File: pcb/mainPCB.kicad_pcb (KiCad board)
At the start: 4 copper layers, 160 x 73.2 mm, 167 parts, among them IC1 FXL6408UMX, IC2 ATA6561-GAQW-N, IC3 ICL3221EIVZ, J1 PTSM-Header-Horizontal-6, J10 Conn_01x08_Female, J11 Conn_01x08_Female, J12 Conn_02x02_Odd_Even, J13 SM04B-SRSS-TB(LF)(SN), J14 USB_B_Micro, J15 RJ45_Amphenol_RJMG1BD3B8K1ANR, J16 DB9_Male_MountingHoles, J17 SM04B-SRSS-TB(LF)(SN), J18 PTSM-Header-Horizontal-2, J3 PTSM-Header-Horizontal-7, J4 CCA-Header-Horizontal-4, J5 PTSM-Header-Horizontal-5, J7 Conn_01x04_Male, J8 Conn_01x04_Male, J9 Conn_01x08_Female, K1 CP1SA-12V-Z, K2 CP1SA-12V-Z, Q1 BC817-40,215, Q2 BC817-40,215, SW1 SW_Push, U1 ESP32-WROOM-32, U10 NUD3124LT1G, U11 LAN8720A, U12 LSM9DS1, U2 AZ1117-3.3, U3 VNH7070AS, U4 ADS1115IDGS, U5 VNH7070AS, U6 PCA9306DCTR, U7 TPD3E001DRLR, U8 CP2102N-A01-GQFN24, U9 VNH7070AS

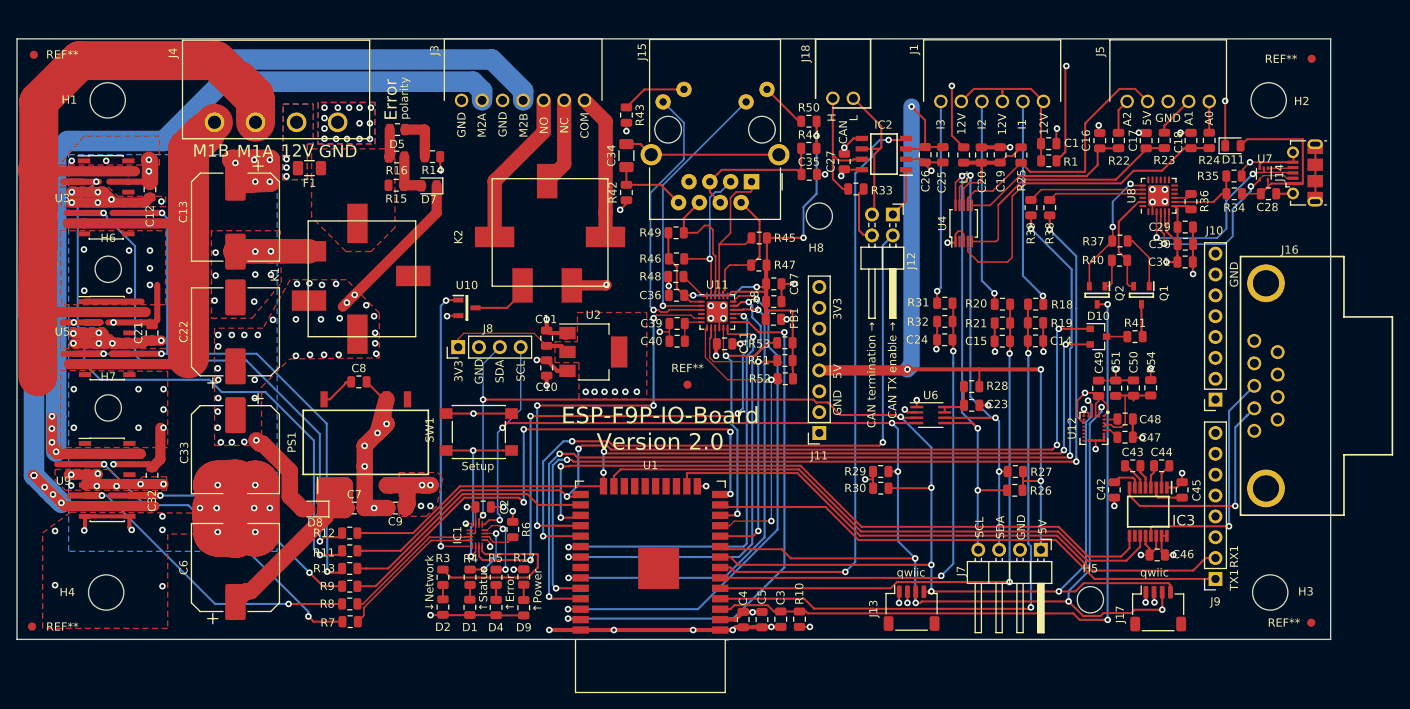
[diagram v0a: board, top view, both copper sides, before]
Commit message: Moved mounting hole. fixes #1
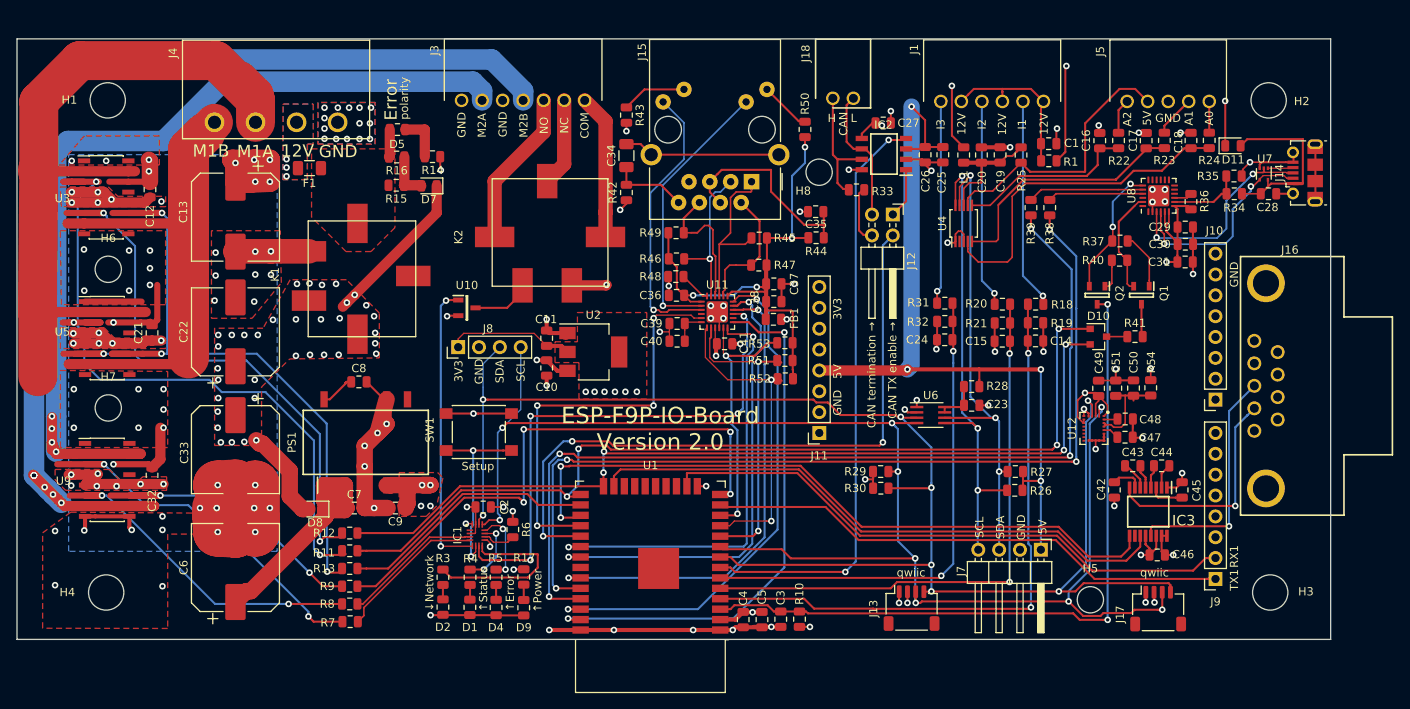
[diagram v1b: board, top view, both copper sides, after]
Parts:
- removed ?: , 
- removed REF** (x5): Fiducial_1mm_Dia_2mm_Outer, Fiducial:Fiducial_1mm_Dia_2mm_Outer
- moved R44 10.9 mm to (114.8, 61.7), turned to 180 degrees
- moved C27 6.66 mm to (123.0, 47.7), turned to 180 degrees
- moved H8 5.35 mm to (115.2, 53.7)
- moved C35 4.61 mm to (114.7, 58.5), turned to 0 degrees
- moved R50 1.10 mm to (113.4, 48.5), turned to 270 degrees
- moved R33 0.12 mm to (119.7, 55.8)
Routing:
- net Net-(C35-Pad2): track 18.3 -> 25.1 mm
- net /LAN8720/+3V3LAN: track 73.6 -> 70.8 mm
- net Net-(IC2-Pad6): track 18.2 -> 17.0 mm
- net Net-(IC2-Pad7): track 16.1 -> 15.1 mm
- net /CAN_RXD: track 73.1 -> 72.5 mm
- net GND: track 280.2 -> 280.4 mm, vias 116 -> 117

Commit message: Minor cleanups
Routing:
- net GND: track 280.4 -> 288.7 mm, vias 117 -> 115
- net +3V3: track 82.3 -> 85.2 mm
- net /CAN_RXD: track 72.5 -> 74.7 mm
- net Net-(IC2-Pad6): track 17.0 -> 18.0 mm, vias 0 -> 1

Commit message: Minor cleanups
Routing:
- net GND: track 288.7 -> 298.2 mm, vias 115 -> 112
- net Net-(C28-Pad1): track 24.5 -> 23.9 mm
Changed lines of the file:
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@@
     (thickness 1.6)
     (drawings 57)
-    (tracks 1815)
+    (tracks 1810)
     (zones 0)
     (modules 161)
@@
   (segment (start 128.0795 52.7685) (end 128.8415 53.5305) (width 0.25) (layer F.Cu) (net 1))
   (segment (start 128.0795 52.5145) (end 130.2385 52.5145) (width 0.25) (layer F.Cu) (net 1))
-  (via (at 159.1945 48.895) (size 0.8) (drill 0.4) (layers F.Cu B.Cu) (net 1))
-  (via (at 154.1145 48.895) (size 0.8) (drill 0.4) (layers F.Cu B.Cu) (net 1))
-  (segment (start 155.1305 48.925) (end 154.1445 48.925) (width 0.25) (layer F.Cu) (net 1))
-  (segment (start 154.1445 48.925) (end 154.1145 48.895) (width 0.25) (layer F.Cu) (net 1))
-  (via (at 149.225 48.006) (size 0.8) (drill 0.4) (layers F.Cu B.Cu) (net 1))
   (via (at 138.43 50.673) (size 0.8) (drill 0.4) (layers F.Cu B.Cu) (net 1))
   (segment (start 134.9375 50.673) (end 138.43 50.673) (width 0.5) (layer F.Cu) (net 1))
@@
   (segment (start 175.62068 50.4198) (end 175.62068 56.8198) (width 0.25) (layer F.Cu) (net 1))
   (segment (start 172.95422 51.29212) (end 172.95422 52.49212) (width 0.25) (layer F.Cu) (net 1))
-  (segment (start 172.02922 52.49212) (end 172.95422 52.49212) (width 0.25) (layer F.Cu) (net 1))
-  (segment (start 168.83672 53.21912) (end 168.83672 52.74412) (width 0.25) (layer F.Cu) (net 1))
-  (segment (start 168.83672 52.74412) (end 169.08872 52.49212) (width 0.25) (layer F.Cu) (net 1))
   (segment (start 170.70372 56.80412) (end 170.70372 56.84012) (width 0.25) (layer F.Cu) (net 1))
   (segment (start 172.91422 56.33212) (end 172.95422 56.29212) (width 0.25) (layer F.Cu) (net 1))
@@
   (segment (start 166.76672 53.37312) (end 167.64772 52.49212) (width 0.2) (layer F.Cu) (net 1))
   (segment (start 166.76672 54.17312) (end 166.76672 53.37312) (width 0.2) (layer F.Cu) (net 1))
-  (segment (start 169.08872 52.49212) (end 169.27322 52.49212) (width 0.25) (layer F.Cu) (net 1))
-  (segment (start 169.27322 52.49212) (end 171.96572 52.49212) (width 0.25) (layer F.Cu) (net 1))
-  (segment (start 167.64772 52.49212) (end 169.27322 52.49212) (width 0.2) (layer F.Cu) (net 1))
-  (via (at 167.64772 52.49212) (size 0.8) (drill 0.4) (layers F.Cu B.Cu) (net 1))
   (via (at 160.7185 66.1035) (size 0.8) (drill 0.4) (layers F.Cu B.Cu) (net 1))
   (segment (start 160.7035 60.3885) (end 160.7035 66.0885) (width 0.25) (layer F.Cu) (net 1))
@@
   (segment (start 149.322 48.895) (end 149.352 48.925) (width 0.25) (layer F.Cu) (net 1))
   (segment (start 149.225 48.798) (end 149.352 48.925) (width 0.25) (layer F.Cu) (net 1))
-  (segment (start 149.225 48.006) (end 149.225 48.798) (width 0.25) (layer F.Cu) (net 1))
   (segment (start 160.4495 48.895) (end 160.4645 48.91) (width 0.25) (layer F.Cu) (net 1))
-  (segment (start 159.1945 48.895) (end 160.4495 48.895) (width 0.25) (layer F.Cu) (net 1))
   (segment (start 129.54 75.176509) (end 129.451436 75.265073) (width 0.25) (layer F.Cu) (net 1))
   (segment (start 129.54 71.882) (end 129.54 75.176509) (width 0.25) (layer F.Cu) (net 1))
@@
   (segment (start 122.633 50.144799) (end 123.90676 48.871039) (width 0.25) (layer F.Cu) (net 1))
   (segment (start 122.633 52.1335) (end 122.633 50.144799) (width 0.25) (layer F.Cu) (net 1))
+  (segment (start 149.908237 49.481237) (end 149.352 48.925) (width 0.25) (layer F.Cu) (net 1))
+  (segment (start 150.27704 49.85004) (end 149.908237 49.481237) (width 0.25) (layer F.Cu) (net 1))
+  (segment (start 160.4645 48.91) (end 159.52446 49.85004) (width 0.25) (layer F.Cu) (net 1))
+  (segment (start 159.52446 49.85004) (end 155.00096 49.85004) (width 0.25) (layer F.Cu) (net 1))
+  (segment (start 155.00096 49.85004) (end 153.95448 49.85004) (width 0.25) (layer F.Cu) (net 1))
+  (segment (start 155.0035 49.8475) (end 155.0035 48.925) (width 0.25) (layer F.Cu) (net 1))
+  (segment (start 153.95448 49.85004) (end 150.27704 49.85004) (width 0.25) (layer F.Cu) (net 1))
+  (via (at 153.95448 49.85004) (size 0.8) (drill 0.4) (layers F.Cu B.Cu) (net 1))
+  (segment (start 168.83672 53.21912) (end 168.83672 52.49212) (width 0.2) (layer F.Cu) (net 1))
+  (segment (start 172.89072 52.49212) (end 168.83672 52.49212) (width 0.25) (layer F.Cu) (net 1))
+  (segment (start 168.83672 52.49212) (end 167.64772 52.49212) (width 0.25) (layer F.Cu) (net 1))
   (via (at 50.292 54.2036) (size 0.8) (drill 0.4) (layers F.Cu B.Cu) (net 2))
   (via (at 50.292 53.1368) (size 0.8) (drill 0.4) (layers F.Cu B.Cu) (net 2))
@@
   (segment (start 167.760769 55.436976) (end 167.760769 56.002661) (width 0.25) (layer B.Cu) (net 97))
   (segment (start 167.760769 56.002661) (end 165.5445 58.21893) (width 0.25) (layer B.Cu) (net 97))
-  (segment (start 169.33672 53.59412) (end 169.33672 53.21912) (width 0.15) (layer F.Cu) (net 98))
-  (segment (start 169.461721 53.719121) (end 169.33672 53.59412) (width 0.15) (layer F.Cu) (net 98))
-  (segment (start 171.992721 53.719121) (end 169.461721 53.719121) (width 0.15) (layer F.Cu) (net 98))
-  (segment (start 172.95422 53.79212) (end 172.12922 53.79212) (width 0.15) (layer F.Cu) (net 98))
-  (segment (start 172.12922 53.79212) (end 172.056221 53.719121) (width 0.15) (layer F.Cu) (net 98))
   (via (at 168.00322 53.91912) (size 0.8) (drill 0.4) (layers F.Cu B.Cu) (net 98))
-  (segment (start 168.178219 53.744121) (end 168.00322 53.91912) (width 0.2) (layer F.Cu) (net 98))
-  (segment (start 169.236719 53.744121) (end 168.178219 53.744121) (width 0.2) (layer F.Cu) (net 98))
-  (segment (start 169.33672 53.21912) (end 169.33672 53.64412) (width 0.2) (layer F.Cu) (net 98))
-  (segment (start 169.33672 53.64412) (end 169.236719 53.744121) (width 0.2) (layer F.Cu) (net 98))
   (via (at 156.2735 61.6585) (size 0.8) (drill 0.4) (layers F.Cu B.Cu) (net 98))
   (segment (start 156.2735 61.6585) (end 156.2735 60.837) (width 0.2) (layer F.Cu) (net 98))
@@
   (segment (start 164.7825 57.13984) (end 164.7825 60.579) (width 0.25) (layer B.Cu) (net 98))
   (segment (start 168.00322 53.91912) (end 164.7825 57.13984) (width 0.25) (layer B.Cu) (net 98))
+  (segment (start 168.568905 53.91912) (end 168.00322 53.91912) (width 0.15) (layer F.Cu) (net 98))
+  (segment (start 168.718914 53.769111) (end 168.568905 53.91912) (width 0.15) (layer F.Cu) (net 98))
+  (segment (start 172.89072 53.79212) (end 172.06572 53.79212) (width 0.15) (layer F.Cu) (net 98))
+  (segment (start 172.06572 53.79212) (end 172.042711 53.769111) (width 0.15) (layer F.Cu) (net 98))
+  (segment (start 169.33672 53.21912) (end 169.33672 53.769111) (width 0.15) (layer F.Cu) (net 98))
+  (segment (start 172.042711 53.769111) (end 169.33672 53.769111) (width 0.15) (layer F.Cu) (net 98))
+  (segment (start 169.33672 53.769111) (end 168.718914 53.769111) (width 0.15) (layer F.Cu) (net 98))
   (segment (start 31.148 88.011) (end 32.512 88.011) (width 1.25) (layer F.Cu) (net 99))
   (segment (start 32.512 88.011) (end 24.482998 88.011) (width 1.25) (layer F.Cu) (net 99))
@@
   (segment (start 169.83672 54.61912) (end 169.83672 55.46612) (width 0.2) (layer F.Cu) (net 177))
   (segment (start 168.97072 56.33212) (end 166.79672 56.33212) (width 0.2) (layer F.Cu) (net 177))
-  (segment (start 167.31742 49.68494) (end 166.51224 50.49012) (width 0.25) (layer F.Cu) (net 177))
-  (segment (start 174.0916 49.68494) (end 167.31742 49.68494) (width 0.25) (layer F.Cu) (net 177))
+  (segment (start 174.0916 50.09896) (end 166.9034 50.09896) (width 0.25) (layer F.Cu) (net 177))
   (segment (start 174.02922 55.09212) (end 174.0916 55.02974) (width 0.25) (layer F.Cu) (net 177))
-  (segment (start 174.0916 55.02974) (end 174.0916 49.68494) (width 0.25) (layer F.Cu) (net 177))
+  (segment (start 166.9034 50.09896) (end 166.51224 50.49012) (width 0.25) (layer F.Cu) (net 177))
+  (segment (start 174.0916 55.02974) (end 174.0916 50.09896) (width 0.25) (layer F.Cu) (net 177))
   (segment (start 84.709002 99.441) (end 84.6455 99.377498) (width 0.15) (layer B.Cu) (net 178))
   (segment (start 84.708998 99.314) (end 84.6455 99.377498) (width 0.25) (layer F.Cu) (net 178))

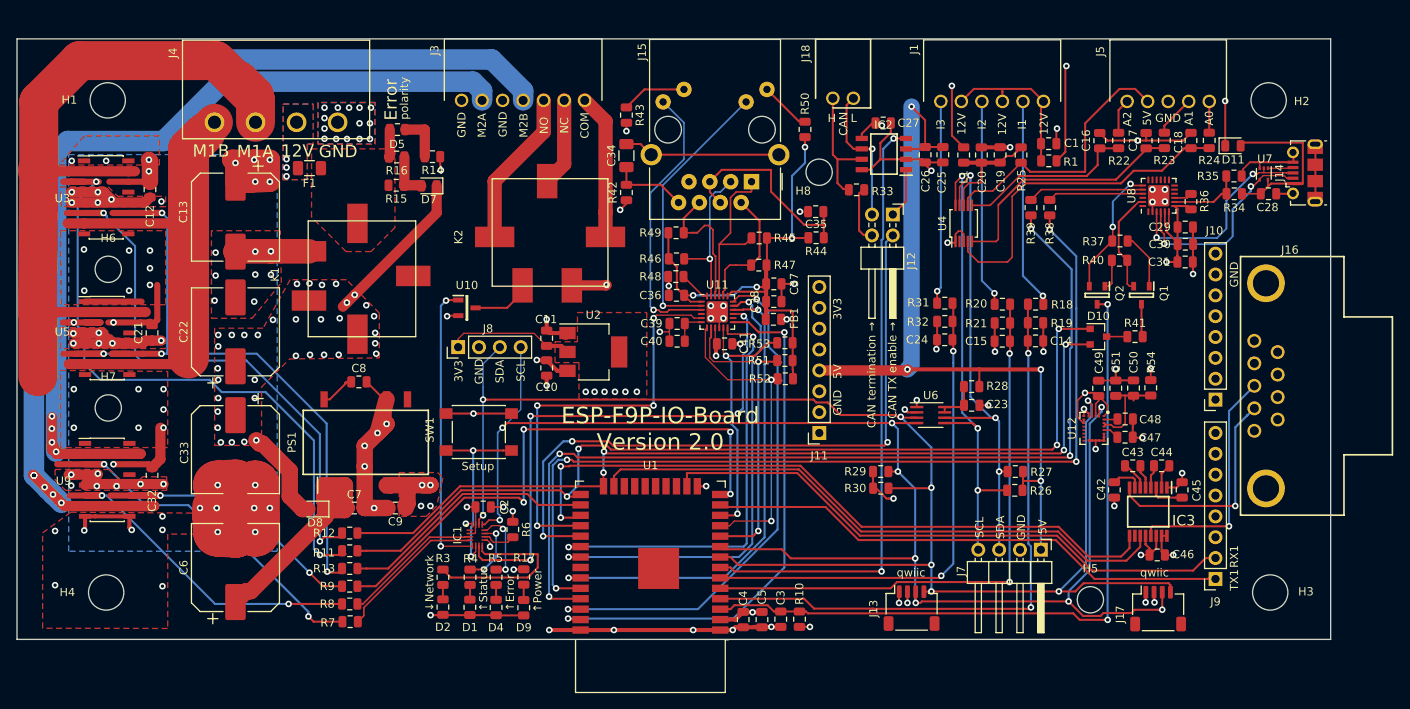
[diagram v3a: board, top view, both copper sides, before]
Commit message: Simplified some tracks
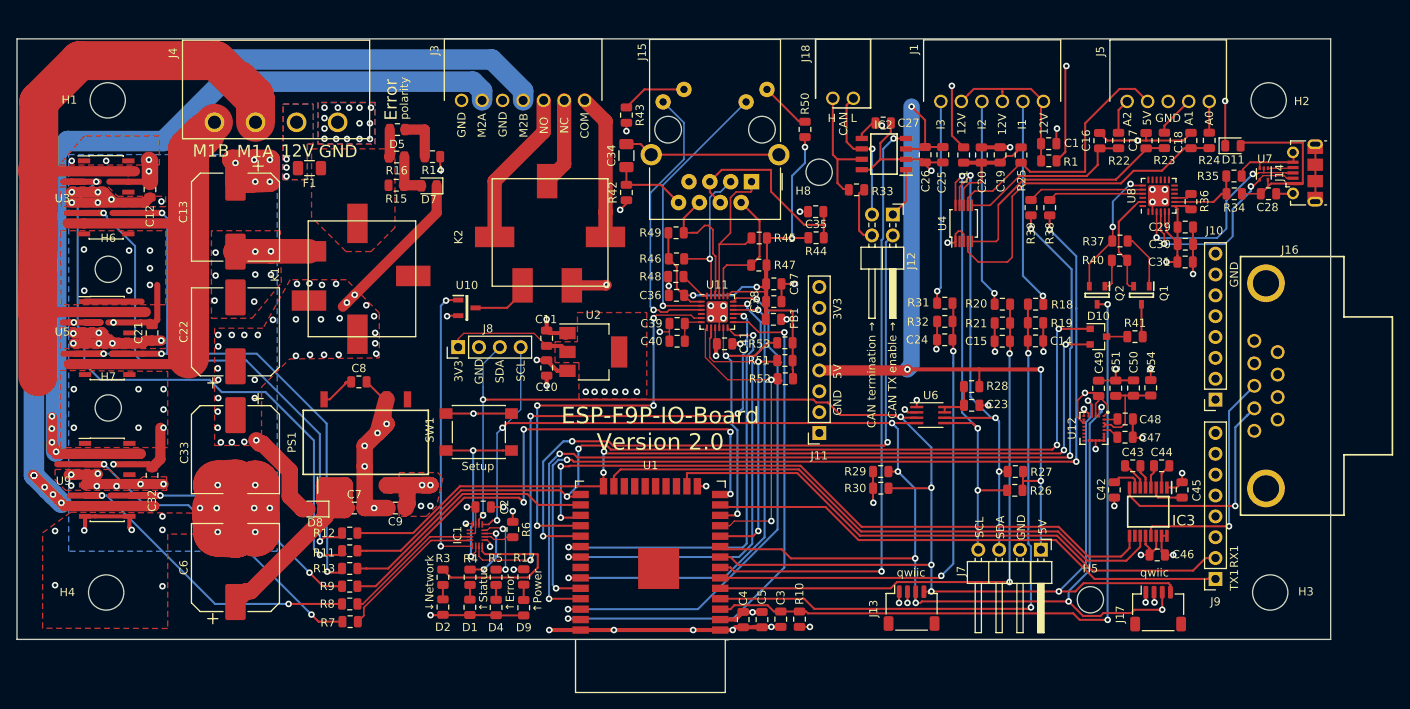
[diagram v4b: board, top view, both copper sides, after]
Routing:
- net /LAN8720/+3V3LAN: track 70.8 -> 66.4 mm
- net +3V3: track 85.2 -> 82.0 mm
- net GND: track 298.2 -> 297.0 mm
- net Net-(C50-Pad2): track 11.6 -> 11.0 mm
